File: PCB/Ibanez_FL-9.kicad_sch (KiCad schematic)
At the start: 156 parts, among them J1 INPUT, J2 OUTPUT, J3 EXT_DC, Q101 2SC2458GR, Q102 2SC2458GR, Q103 2SK44SPC, Q104 2SC2458GR, Q105 2SC2458GR, Q106 2SC2458GR, Q107 2SA1048Y/GR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

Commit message: add custom components; fix all labels
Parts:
- removed Q108A1001, Q108B1001: 2SC1583F, Package_TO_SOT_THT:TO-92Flat, symbol Transistor_BJT:2SC1815
- added Q108: 2SC1583F, Package_TO_SOT_THT:TO-92Flat_5-PIN, symbol Transistor_Array:2SC1583F
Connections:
- net GND: now also Q108.3 (E)
- net at R148.2: now also Q108.4 (C2)
- net at C128.1, R149.2, R151.2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: now also Q108.5 (B2)
- net CP14: now reaches C121.2, D103.1 (K), R133.1
- net at R149.1, R150.1: now also Q108.1 (B1), Q108.2 (C1)
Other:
- moved on the sheet: C128, R148, R149, R150, R151, R152, R153, RV101

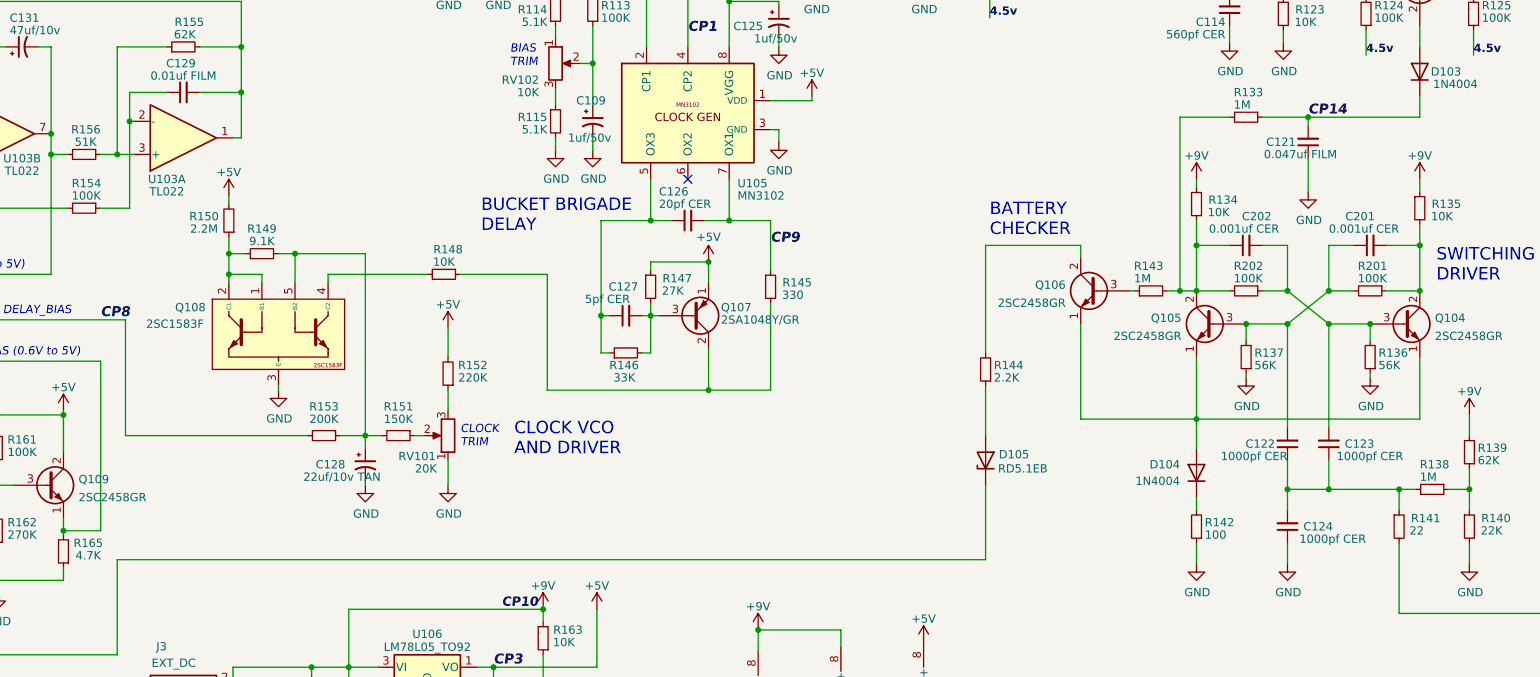
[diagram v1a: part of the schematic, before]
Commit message: update test points; add hybrid devices
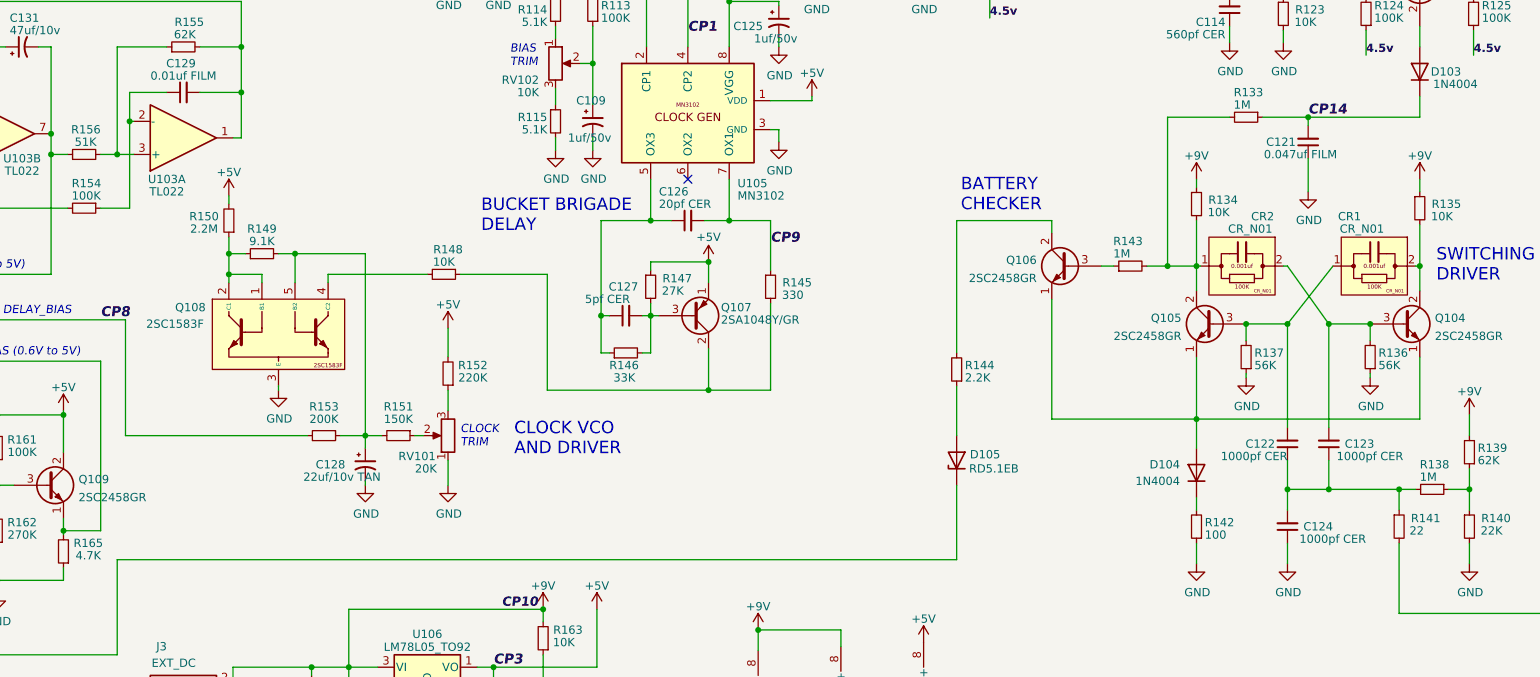
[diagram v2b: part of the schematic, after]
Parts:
- removed C201, C202: 0.001uf CER, Capacitor_THT:C_Disc_D3.0mm_W2.0mm_P2.50mm, symbol Device:C_Small
- removed R201, R202: 100K, Resistor_THT:R_Axial_DIN0204_L3.6mm_D1.6mm_P2.54mm_Vertical, symbol Device:R_Small
- added CR1, CR2: CR_N01, Capacitor_THT:C_Disc_D5.0mm_W2.5mm_P2.50mm, symbol Device:CR_N01
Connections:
- net at C123.2, Q104.3 (B), R136.2: now also CR2.2
- net at Q105.2 (C), R133.2, R134.2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: now also CR2.1
- net at C122.2, Q105.3 (B), R137.2: now also CR1.1
- net at Q104.2 (C), R135.2: now also CR1.2
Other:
- moved on the sheet: D105, Q106, R143, R144

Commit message: update docs
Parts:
- D101, D102, D103, D104, D107: value 1N4004 -> 1N4148

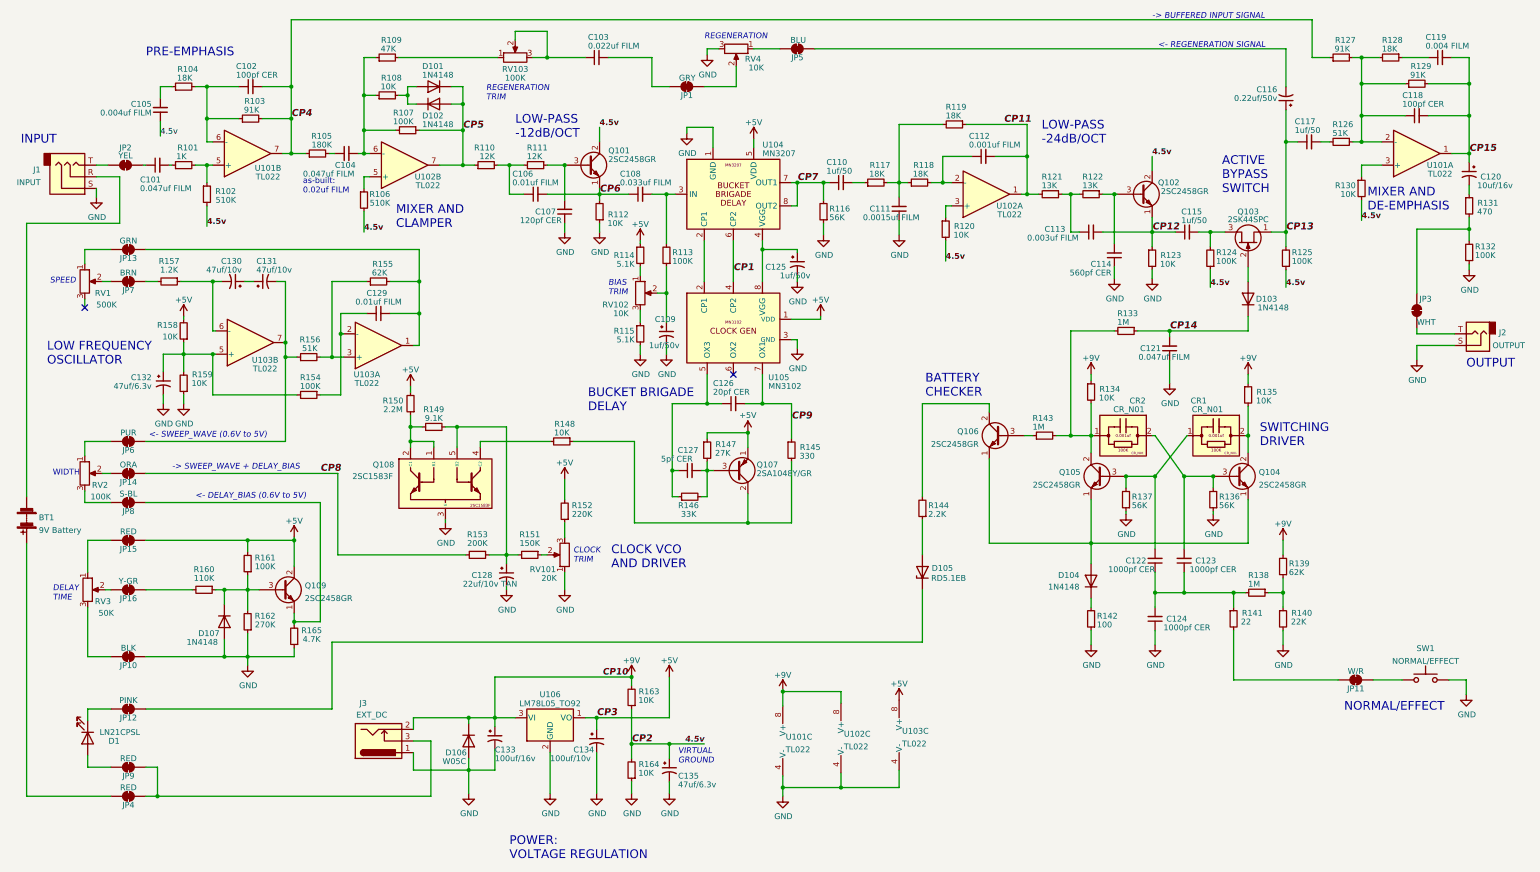
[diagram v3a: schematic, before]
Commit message: update board layout and docs
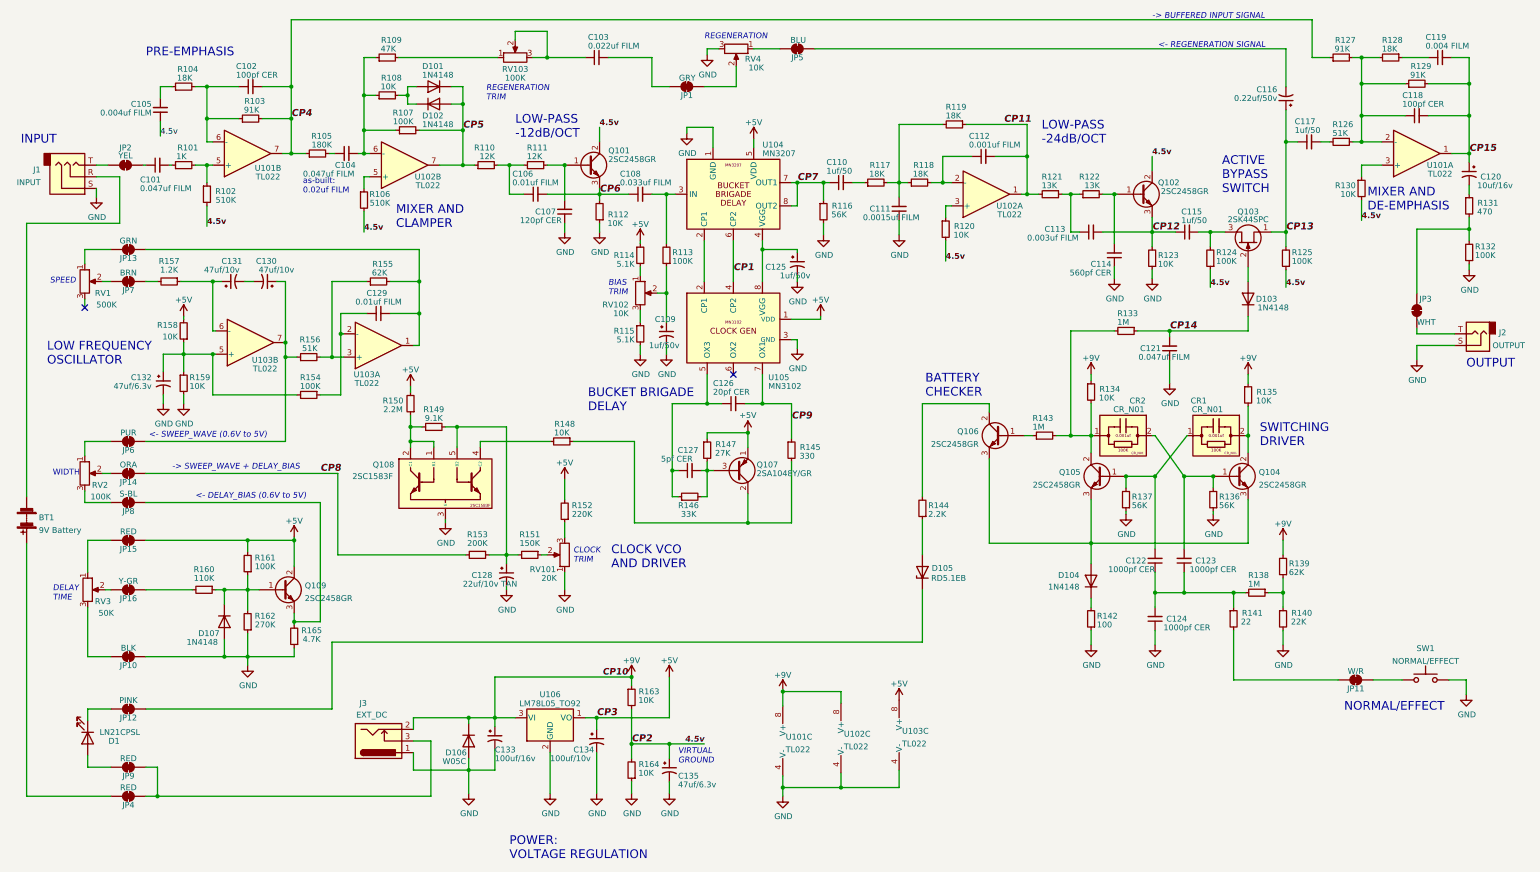
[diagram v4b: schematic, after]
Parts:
- C101: footprint Capacitor_THT:C_Rect_L7.2mm_W3.5mm_P5.00mm_FKS2_FKP2_MKS2_MKP2 -> Capacitor_THT:C_Rect_L7.0mm_W2.0mm_P5.00mm
- C103, C104, C105, C108, C111, C112, C113, C119, C129: footprint Capacitor_THT:C_Rect_L7.0mm_W2.0mm_P5.00mm -> Capacitor_THT:C_Rect_L4.6mm_W2.0mm_P2.50mm_MKS02_FKP02
- C106, C121: footprint Capacitor_THT:C_Rect_L7.0mm_W2.5mm_P5.00mm -> Capacitor_THT:C_Rect_L4.6mm_W2.0mm_P2.50mm_MKS02_FKP02
- C116, C120: footprint Capacitor_THT:CP_Radial_D5.0mm_P2.50mm -> Capacitor_THT:CP_Radial_D4.0mm_P2.00mm
- C130: renamed from C131; footprint Capacitor_THT:CP_Radial_D5.0mm_P2.50mm -> Capacitor_THT:CP_Radial_D4.0mm_P2.00mm
- C131: renamed from C130; footprint Capacitor_THT:CP_Radial_D5.0mm_P2.50mm -> Capacitor_THT:CP_Radial_D4.0mm_P2.00mm
- Q101, Q102, Q104, Q105, Q106, Q109: symbol Transistor_BJT:2SC1815 -> Transistor_BJT:2SD1047
- U106: footprint Package_TO_SOT_THT:TO-92_Inline -> Package_TO_SOT_THT:TO-92
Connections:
- net +9V: now also R163.1; no longer R163.2
- net 4.5v: now also R163.2; no longer R163.1
- net CP12: now also Q102.3 (E), R123.2; no longer Q102.1 (E), R123.1
- net CP5: now also R107.2; no longer R107.1
- net CP6: now also Q101.3 (E); no longer Q101.1 (E)
- net CP7: now also R116.1; no longer R116.2
- net GND: now also R116.2, R123.1, R159.2; no longer R116.1, R123.2, R159.1
- net at D107.1 (K), R160.1, R161.1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: now also Q109.1 (B); no longer Q109.3 (B)
- net at C107.2, R111.1: now also Q101.1 (B); no longer Q101.3 (B)
- net at C123.2, CR2.2, R136.2: now also Q104.1 (B); no longer Q104.3 (B)
- net at R143.1: now also Q106.1 (B); no longer Q106.3 (B)
- net at C132.1, R154.2, R158.1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: now also R159.1; no longer R159.2
- net at C104.2, R108.1, R109.1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: now also R107.1; no longer R107.2
- net at C113.1, R121.1: now also R122.1; no longer R122.2
- net at C130.1: now also JP6.2 (B), R156.1, U103.7; no longer C131.1
- net at C122.2, CR1.1, R137.2: now also Q105.1 (B); no longer Q105.3 (B)
- net at R157.1, U103.6 (-): now also C131.1; no longer C131.2
- net at JP8.2 (B), R165.2: now also Q109.3 (E); no longer Q109.1 (E)
- new net: D104.2 (A), Q104.3 (E), Q105.3 (E), Q106.3 (E)
- new net: C114.2, Q102.1 (B), R122.2
- new net: C130.2, C131.2
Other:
- moved on the sheet: C130, C131, R107, R116, R122, R123, R159, R163

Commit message: update docs
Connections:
- net CP8: now also R153.1; no longer R153.2
- net at C128.1, Q108.5 (B2), R149.2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: now also R153.2; no longer R153.1
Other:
- moved on the sheet: R153
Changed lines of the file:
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@@
   (title_block
     (title "Ibanez_FL-9_Flanger_Pedal MP-FL0601")
-    (date "2022-11-24")
+    (date "2022-11-25")
     (rev "v02")
     (company "Cedar Grove Studios")
@@
     (pin "2")
   )
-  (symbol (lib_id "Device:R_Small") (at 114.3 131.445 270) (unit 1)
+  (symbol (lib_id "Device:R_Small") (at 114.3 131.445 90) (unit 1)
     (in_bom yes) (on_board yes)
-    (property "Reference" "R153" (id 0) (at 114.3 127 90))
-    (property "Value" "200K" (id 1) (at 114.3 128.905 90))
+    (property "Reference" "R153" (id 0) (at 114.935 127.635 90))
+    (property "Value" "200K" (id 1) (at 114.935 129.54 90))
     (property "Footprint" "Resistor_THT:R_Axial_DIN0204_L3.6mm_D1.6mm_P2.54mm_Vertical" (id 2) (at 114.3 131.445 0)
       (effects (font (size 1.27 1.27)) hide)
@@
   (symbol (lib_id "Device:CP1_Small") (at 120.65 135.89 0) (unit 1)
     (in_bom yes) (on_board yes)
-    (property "Reference" "C128" (id 0) (at 113.03 135.89 0)
+    (property "Reference" "C128" (id 0) (at 113.665 135.89 0)
       (effects (font (size 1.27 1.27)) (justify left))
     )

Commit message: update schematic, guide, and docs
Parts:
- renumbered U101 to IC101, U102 to IC102, U103 to IC103, U104 to IC104, U105 to IC105, U106 to IC106
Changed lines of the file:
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@@
   (title_block
     (title "Ibanez_FL-9_Flanger_Pedal MP-FL0601")
-    (date "2022-11-25")
+    (date "2022-11-26")
     (rev "v02")
     (company "Cedar Grove Studios")
@@
   (symbol (lib_id "Amplifier_Operational:TL072") (at 92.71 85.725 0) (mirror x) (unit 1)
     (in_bom yes) (on_board yes)
-    (property "Reference" "U103" (id 0) (at 90.17 92.075 0))
+    (property "Reference" "IC103" (id 0) (at 90.17 92.075 0))
     (property "Value" "TL022" (id 1) (at 90.17 93.98 0))
     (property "Footprint" "Package_DIP:DIP-8_W7.62mm" (id 2) (at 92.71 85.725 0)
@@
   (symbol (lib_id "Timer:MN3102") (at 170.18 81.915 0) (unit 1)
     (in_bom yes) (on_board yes)
-    (property "Reference" "U105" (id 0) (at 177.8 92.71 0)
+    (property "Reference" "IC105" (id 0) (at 177.8 92.71 0)
       (effects (font (size 1.27 1.27)) (justify left))
     )
@@
   (symbol (lib_id "Amplifier_Operational:TL072") (at 98.425 46.355 0) (mirror x) (unit 2)
     (in_bom yes) (on_board yes)
-    (property "Reference" "U102" (id 0) (at 103.505 48.895 0))
+    (property "Reference" "IC102" (id 0) (at 103.505 48.895 0))
     (property "Value" "TL022" (id 1) (at 103.505 50.8 0))
     (property "Footprint" "Package_DIP:DIP-8_W7.62mm" (id 2) (at 98.425 46.355 0)
@@
   (symbol (lib_id "Amplifier_Operational:TL072") (at 319.405 43.815 0) (mirror x) (unit 1)
     (in_bom yes) (on_board yes)
-    (property "Reference" "U101" (id 0) (at 324.485 46.355 0))
+    (property "Reference" "IC101" (id 0) (at 324.485 46.355 0))
     (property "Value" "TL022" (id 1) (at 324.485 48.26 0))
     (property "Footprint" "Package_DIP:DIP-8_W7.62mm" (id 2) (at 319.405 43.815 0)
@@
   (symbol (lib_id "Amplifier_Operational:TL072") (at 64.77 85.09 0) (mirror x) (unit 2)
     (in_bom yes) (on_board yes)
-    (property "Reference" "U103" (id 0) (at 67.945 88.9 0))
+    (property "Reference" "IC103" (id 0) (at 67.945 88.9 0))
     (property "Value" "TL022" (id 1) (at 67.945 90.805 0))
     (property "Footprint" "Package_DIP:DIP-8_W7.62mm" (id 2) (at 64.77 85.09 0)
@@
   (symbol (lib_id "Regulator_Linear:LM78L05_TO92") (at 130.175 167.005 0) (unit 1)
     (in_bom yes) (on_board yes)
-    (property "Reference" "U106" (id 0) (at 130.175 161.925 0))
+    (property "Reference" "IC106" (id 0) (at 130.175 161.925 0))
     (property "Value" "LM78L05_TO92" (id 1) (at 130.175 163.9086 0))
     (property "Footprint" "Package_TO_SOT_THT:TO-92" (id 2) (at 130.175 161.29 0)
@@
   (symbol (lib_id "Audio:MN3207") (at 170.18 52.705 0) (unit 1)
     (in_bom yes) (on_board yes)
-    (property "Reference" "U104" (id 0) (at 176.53 41.91 0)
+    (property "Reference" "IC104" (id 0) (at 176.53 41.91 0)
       (effects (font (size 1.27 1.27)) (justify left))
     )
@@
   (symbol (lib_id "Amplifier_Operational:TL072") (at 64.135 43.815 0) (mirror x) (unit 2)
     (in_bom yes) (on_board yes)
-    (property "Reference" "U101" (id 0) (at 68.58 46.99 0))
+    (property "Reference" "IC101" (id 0) (at 68.58 46.99 0))
     (property "Value" "TL022" (id 1) (at 68.58 48.895 0))
     (property "Footprint" "Package_DIP:DIP-8_W7.62mm" (id 2) (at 64.135 43.815 0)
@@
   (symbol (lib_id "Amplifier_Operational:TL072") (at 225.425 52.705 0) (mirror x) (unit 1)
     (in_bom yes) (on_board yes)
-    (property "Reference" "U102" (id 0) (at 230.505 55.245 0))
+    (property "Reference" "IC102" (id 0) (at 230.505 55.245 0))
     (property "Value" "TL022" (id 1) (at 230.505 57.15 0))
     (property "Footprint" "Package_DIP:DIP-8_W7.62mm" (id 2) (at 225.425 52.705 0)
@@
       (reference "D107") (unit 1) (value "1N4148") (footprint "Diode_THT:D_T-1_P2.54mm_Vertical_KathodeUp")
     )
+    (path "/deeba859-c930-4a16-bb4d-94b435567fd8"
+      (reference "IC101") (unit 1) (value "TL022") (footprint "Package_DIP:DIP-8_W7.62mm")
+    )
+    (path "/f76cbbe5-85eb-46c7-823a-15d6d832a075"
+      (reference "IC101") (unit 2) (value "TL022") (footprint "Package_DIP:DIP-8_W7.62mm")
+    )
+    (path "/fc8ffd4f-592d-4600-af07-01b564606849"
+      (reference "IC102") (unit 1) (value "TL022") (footprint "Package_DIP:DIP-8_W7.62mm")
+    )
+    (path "/bfe8d056-0a28-4d98-90fb-99d88dacefd2"
+      (reference "IC102") (unit 2) (value "TL022") (footprint "Package_DIP:DIP-8_W7.62mm")
+    )
+    (path "/156cc437-73f9-4b3d-899d-c1d51a8c376d"
+      (reference "IC103") (unit 1) (value "TL022") (footprint "Package_DIP:DIP-8_W7.62mm")
+    )
+    (path "/e7d51f6e-827f-46b1-9000-d82927f2da13"
+      (reference "IC103") (unit 2) (value "TL022") (footprint "Package_DIP:DIP-8_W7.62mm")
+    )
+    (path "/ed34a539-454e-41b2-957f-a6259baf48fe"
+      (reference "IC104") (unit 1) (value "MN3207") (footprint "Package_DIP:DIP-8_W7.62mm")
+    )
+    (path "/2b37b547-d985-4bb1-95e9-f10600c4d410"
+      (reference "IC105") (unit 1) (value "MN3102") (footprint "Package_DIP:DIP-8_W7.62mm")
+    )
+    (path "/e92869d9-a188-4eb9-8392-4ed107683702"
+      (reference "IC106") (unit 1) (value "LM78L05_TO92") (footprint "Package_TO_SOT_THT:TO-92")
+    )
     (path "/71be4c6e-79e7-4078-aa44-d0f9f3717533"
       (reference "J1") (unit 1) (value "INPUT") (footprint "")
@@
       (reference "SW1") (unit 1) (value "NORMAL/EFFECT") (footprint "")
     )
-    (path "/deeba859-c930-4a16-bb4d-94b435567fd8"
-      (reference "U101") (unit 1) (value "TL022") (footprint "Package_DIP:DIP-8_W7.62mm")
-    )
-    (path "/f76cbbe5-85eb-46c7-823a-15d6d832a075"
-      (reference "U101") (unit 2) (value "TL022") (footprint "Package_DIP:DIP-8_W7.62mm")
-    )
     (path "/c0238134-b46d-42a1-9fdb-86790b8a110e"
       (reference "U101") (unit 3) (value "TL022") (footprint "Package_DIP:DIP-8_W7.62mm")
     )
-    (path "/fc8ffd4f-592d-4600-af07-01b564606849"
-      (reference "U102") (unit 1) (value "TL022") (footprint "Package_DIP:DIP-8_W7.62mm")
-    )
-    (path "/bfe8d056-0a28-4d98-90fb-99d88dacefd2"
-      (reference "U102") (unit 2) (value "TL022") (footprint "Package_DIP:DIP-8_W7.62mm")
-    )
     (path "/37322642-a9e8-4b7a-994e-382297571ca4"
       (reference "U102") (unit 3) (value "TL022") (footprint "Package_DIP:DIP-8_W7.62mm")
     )
-    (path "/156cc437-73f9-4b3d-899d-c1d51a8c376d"
-      (reference "U103") (unit 1) (value "TL022") (footprint "Package_DIP:DIP-8_W7.62mm")
-    )
-    (path "/e7d51f6e-827f-46b1-9000-d82927f2da13"
-      (reference "U103") (unit 2) (value "TL022") (footprint "Package_DIP:DIP-8_W7.62mm")
-    )
     (path "/80bbc5b6-fa99-4be6-8706-175bfe844748"
       (reference "U103") (unit 3) (value "TL022") (footprint "Package_DIP:DIP-8_W7.62mm")
     )
-    (path "/ed34a539-454e-41b2-957f-a6259baf48fe"
-      (reference "U104") (unit 1) (value "MN3207") (footprint "Package_DIP:DIP-8_W7.62mm")
-    )
-    (path "/2b37b547-d985-4bb1-95e9-f10600c4d410"
-      (reference "U105") (unit 1) (value "MN3102") (footprint "Package_DIP:DIP-8_W7.62mm")
-    )
-    (path "/e92869d9-a188-4eb9-8392-4ed107683702"
-      (reference "U106") (unit 1) (value "LM78L05_TO92") (footprint "Package_TO_SOT_THT:TO-92")
-    )
   )

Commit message: update PCB and docs
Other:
- note added: "C116 upgraded to FILM 2022-11-26"
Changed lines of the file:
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@@
   (title_block
     (title "Ibanez_FL-9_Flanger_Pedal MP-FL0601")
-    (date "2022-11-26")
-    (rev "v02")
+    (date "2022-11-29")
+    (rev "1.0.0")
     (company "Cedar Grove Studios")
     (comment 1 "MP-FL0601")
@@
     (effects (font (size 1.27 1.27) italic) (justify left bottom))
   )
+  (text "C116 upgraded to FILM\n2022-11-26\n" (at 265.43 29.21 0)
+    (effects (font (size 1.27 1.27)) (justify left bottom))
+  )
   (text "NORMAL/EFFECT" (at 303.53 165.735 0)
